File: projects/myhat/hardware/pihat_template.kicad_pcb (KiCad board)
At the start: 2 copper layers, 65 x 56.5 mm, 37 parts, among them P1 CONN_01X02, P2 CONN_01X02, P3 Raspberry_Pi_+_Conn, Q1 BSS138, U1 LM3489, U2 CAT24C32HU4I-GT3, U3 FDC5614P, U4 LM1117IMPX-ADJ, U5 DMMT5401

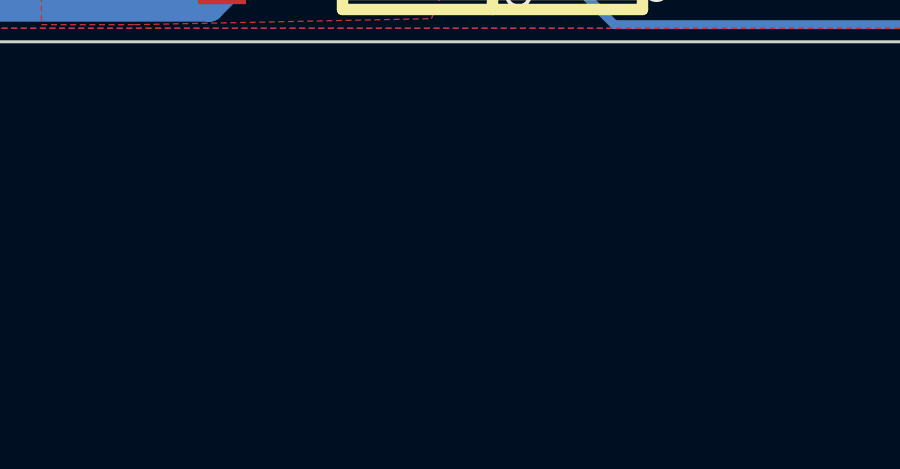
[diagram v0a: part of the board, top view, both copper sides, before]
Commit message: Added footprint for MAX17205
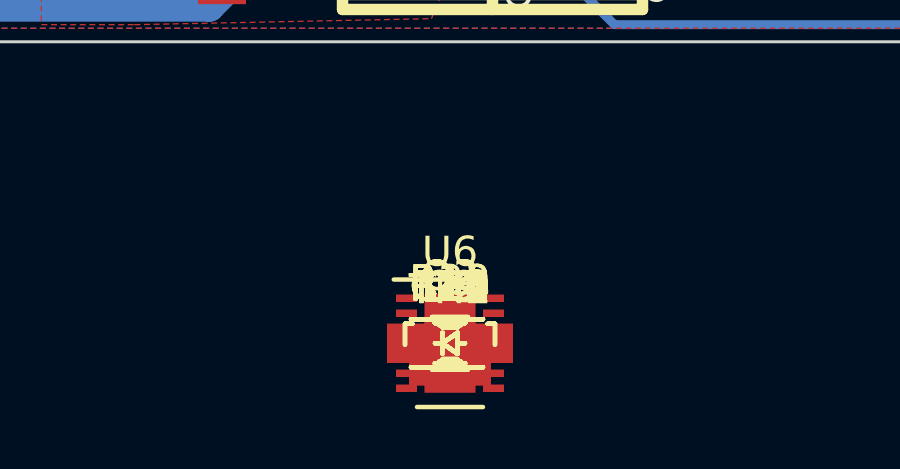
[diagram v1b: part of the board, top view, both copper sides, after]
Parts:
- added C10, C11: 0.47uF, Capacitors_SMD:C_0603_HandSoldering, F.Cu at (137.4, 137.6)
- added C9: 1uF, Capacitors_SMD:C_0603_HandSoldering, F.Cu at (137.4, 137.6)
- added D2: 18V, Diodes_SMD:SOD-323, F.Cu at (137.4, 137.6)
- added D4, D5, D6: 5.6V, Diodes_SMD:SOD-323, F.Cu at (137.4, 137.6)
- added Q2, Q3: BSS138, TO_SOT_Packages_SMD:SOT-23, F.Cu at (137.4, 137.6)
- added R13: 2.0M, Resistors_SMD:R_0805_HandSoldering, F.Cu at (137.4, 137.6)
- added R14: 300K, Resistors_SMD:R_0603_HandSoldering, F.Cu at (137.4, 137.6)
- added R15: 200k, Resistors_SMD:R_0603_HandSoldering, F.Cu at (137.4, 137.6)
- added R16, R17: 10K, Resistors_SMD:R_0603_HandSoldering, F.Cu at (137.4, 137.6)
- added R18: 510K, Resistors_SMD:R_0603_HandSoldering, F.Cu at (137.4, 137.6)
- added R19: 1M, Resistors_SMD:R_0603_HandSoldering, F.Cu at (137.4, 137.6)
- added R20: 0.01, Resistors_SMD:R_0805_HandSoldering, F.Cu at (137.4, 137.6)
- added R21: 1K, Resistors_SMD:R_0603_HandSoldering, F.Cu at (137.4, 137.6)
- added R22, R23: 150, Resistors_SMD:R_0603_HandSoldering, F.Cu at (137.4, 137.6)
- added TH1, TH2: 10K NTC, Resistors_SMD:R_0402, F.Cu at (137.4, 137.6)
- added U6: MAX17205, Housings_DFN_QFN:DFN-14-1EP_3x4mm_Pitch0.5mm, F.Cu at (137.4, 137.6)
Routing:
- net GND: track 280.5 -> 301.3 mm
- net +5V: track 75.5 -> 54.7 mm
